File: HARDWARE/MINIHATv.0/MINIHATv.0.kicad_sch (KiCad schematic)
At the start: 9 parts, among them J1 USB_C_Receptacle_PowerOnly_6P, U1 MIC5504-3.3YM5

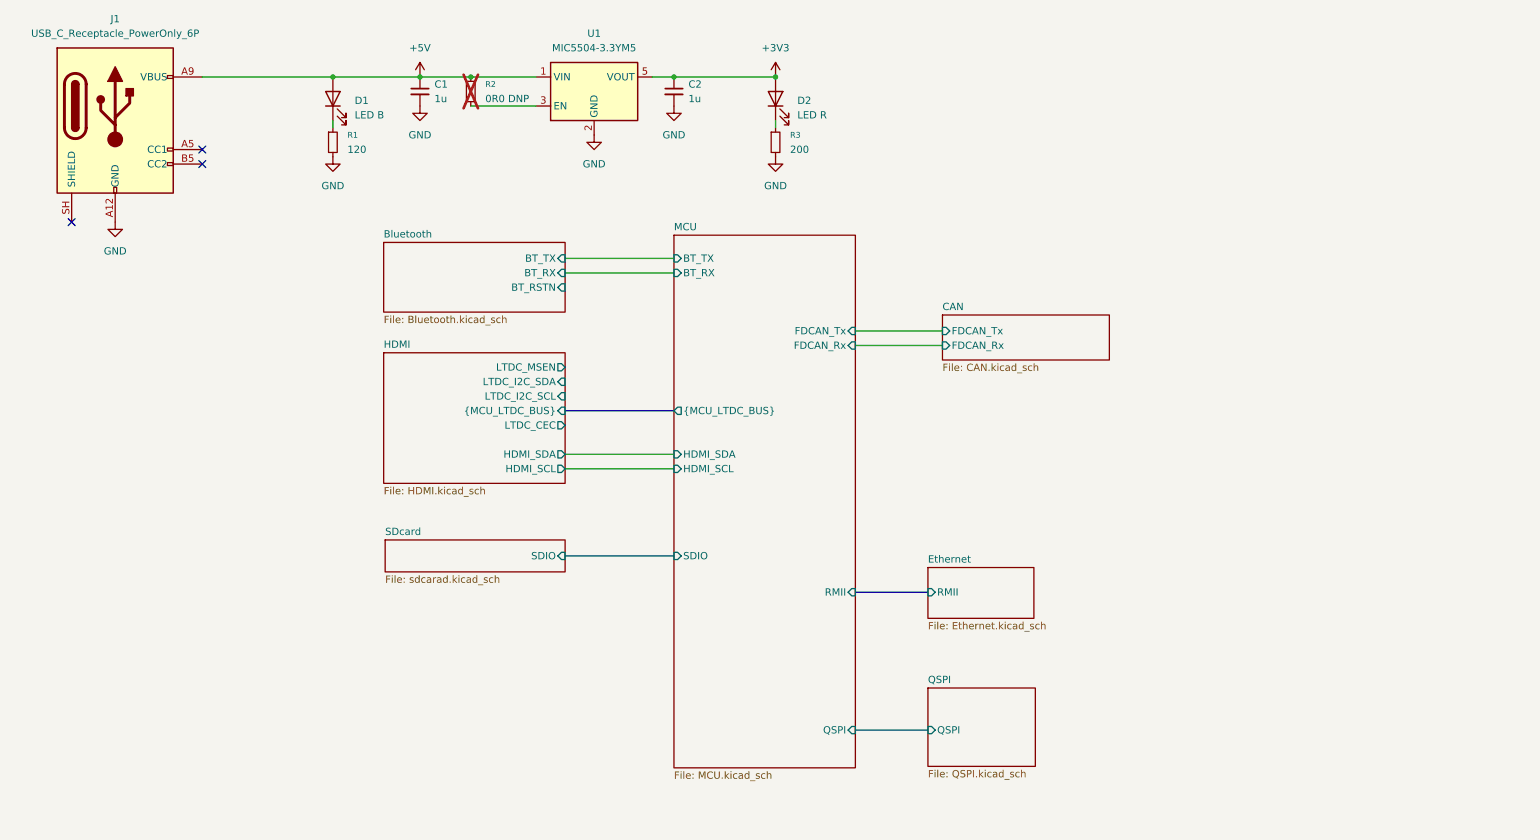
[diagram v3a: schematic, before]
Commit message: added sdram and usb pages to top page
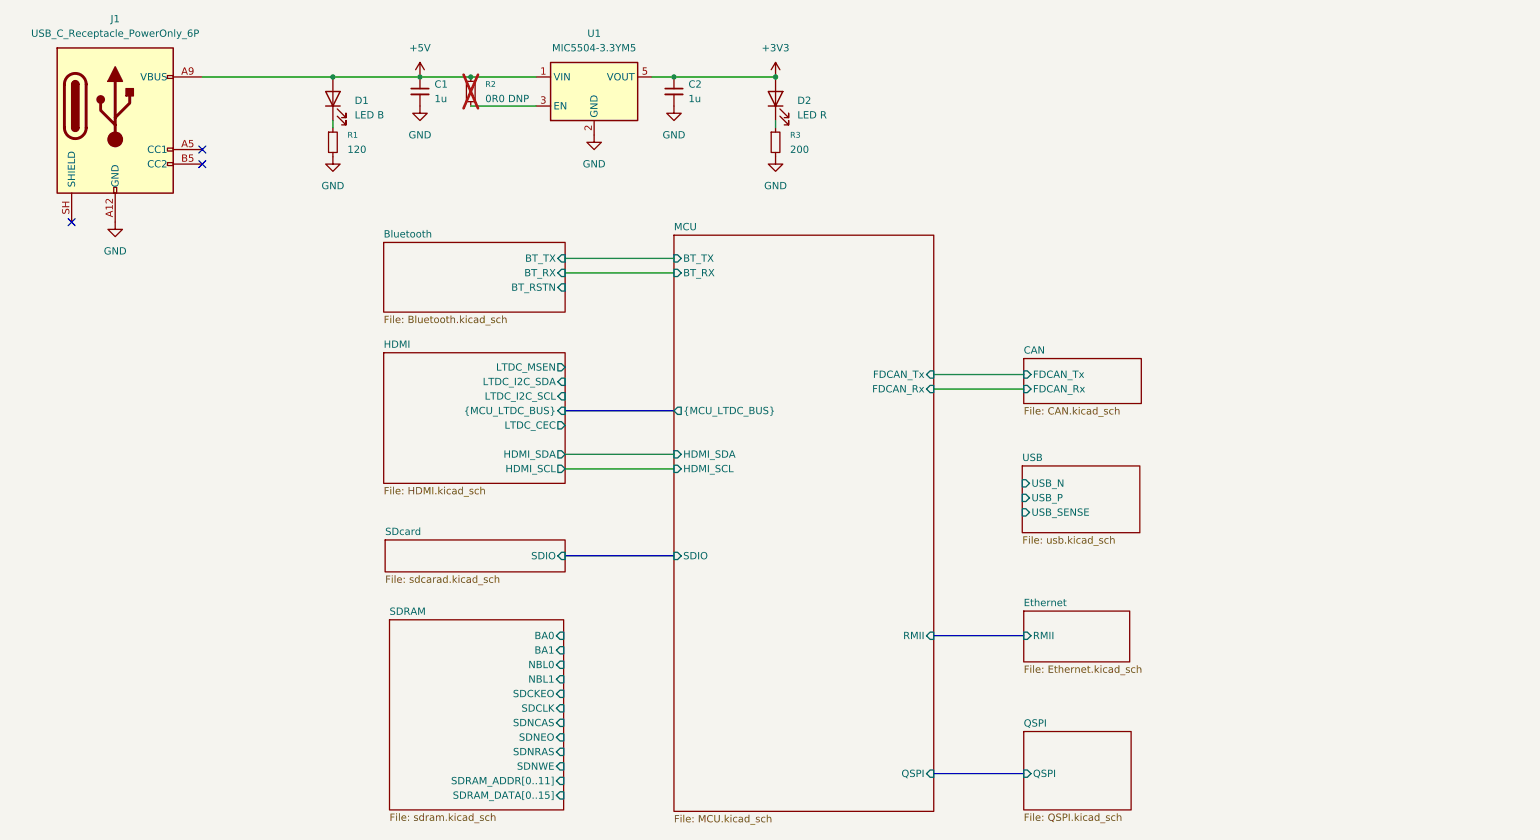
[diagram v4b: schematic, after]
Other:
- added sheet SDRAM (sdram.kicad_sch)
- added sheet USB (usb.kicad_sch)

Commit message: added ltdc bus to mcu page, editoral change to rmii bus
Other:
- sheet Ethernet ports: added ETH_RESET, {RMII}; removed RMII
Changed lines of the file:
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@@
 	(sheet
 		(at 189.484 117.602)
-		(size 18.542 8.89)
+		(size 18.542 10.922)
 		(exclude_from_sim no)
 		(in_bom yes)
@@
 		)
 		(property "Sheetfile" "Ethernet.kicad_sch"
-			(at 189.484 127.0766 0)
+			(at 189.484 129.1086 0)
 			(show_name no)
 			(do_not_autoplace no)
@@
 			)
 		)
-		(pin "RMII" input
+		(pin "ETH_RESET" input
+			(at 189.484 124.46 180)
+			(effects
+				(font
+					(size 1.27 1.27)
+				)
+				(justify left)
+			)
+		)
+		(pin "{RMII}" input
 			(at 189.484 121.92 180)
 			(effects

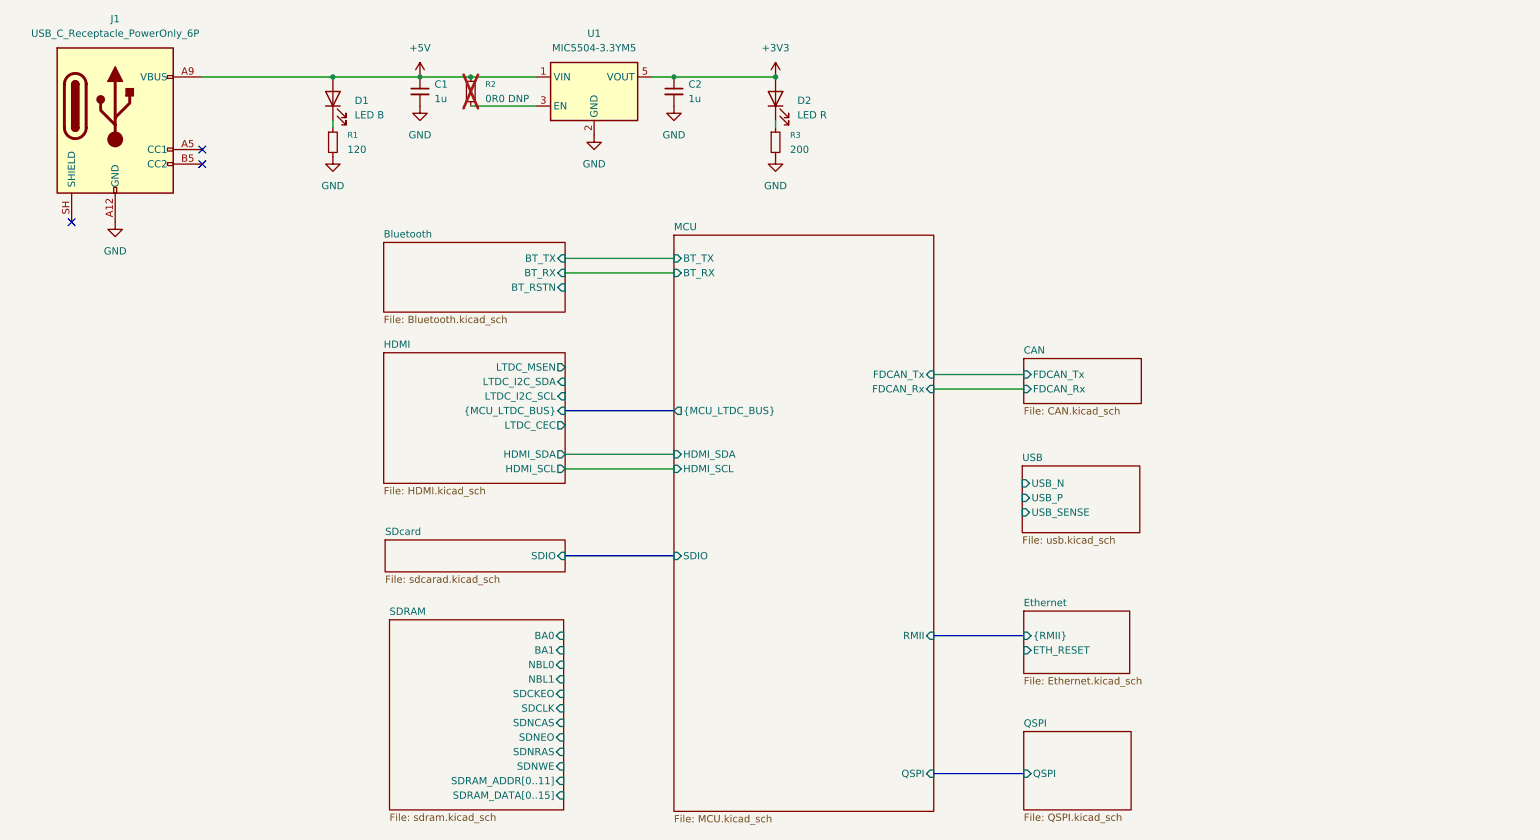
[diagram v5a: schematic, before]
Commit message: connecting i2c and uart bt/hdmi
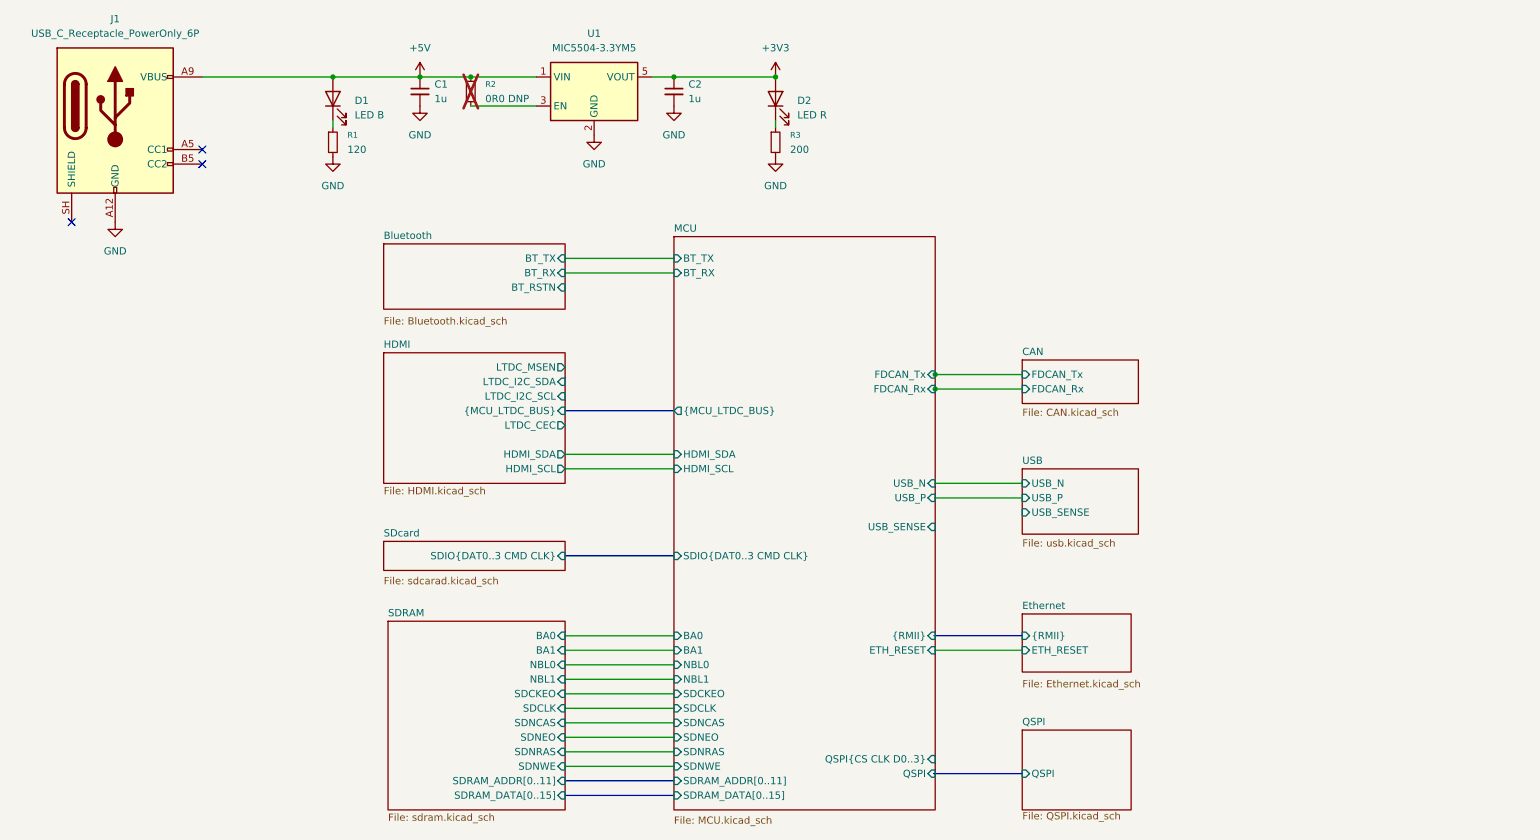
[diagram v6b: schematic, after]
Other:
- sheet MCU ports: added BA0, BA1, ETH_RESET, NBL0, NBL1, QSPI{CS CLK D0..3}, SDCKEO, SDCLK, SDIO{DAT0..3 CMD CLK}, SDNCAS, SDNEO, SDNRAS, SDNWE, SDRAM_ADDR[0..11], SDRAM_DATA[0..15], USB_N, USB_P, USB_SENSE, {RMII}; removed RMII, SDIO
- sheet SDcard ports: added SDIO{DAT0..3 CMD CLK}; removed SDIO

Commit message: mcu pwr/vcap ports, hdmi gpio, buses
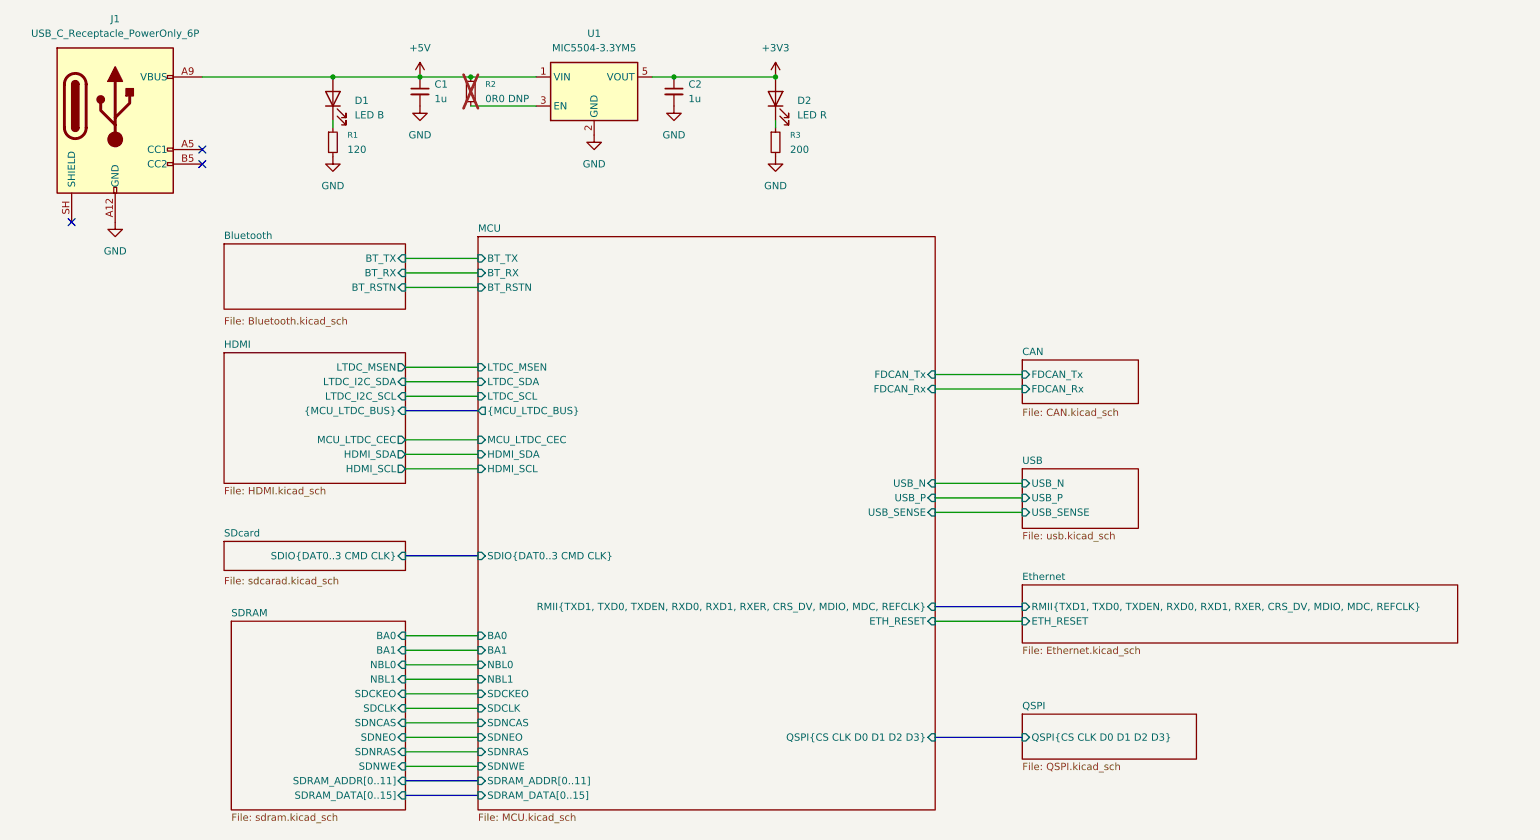
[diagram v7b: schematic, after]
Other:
- sheet Ethernet ports: added RMII{TXD1, TXD0, TXDEN, RXD0, RXD1, RXER, CRS_DV, MDIO, MDC, REFCLK}; removed {RMII}
- sheet HDMI ports: added MCU_LTDC_CEC; removed LTDC_CEC
- sheet MCU ports: added BT_RSTN, LTDC_MSEN, LTDC_SCL, LTDC_SDA, MCU_LTDC_CEC, QSPI{CS CLK D0 D1 D2 D3}, RMII{TXD1, TXD0, TXDEN, RXD0, RXD1, RXER, CRS_DV, MDIO, MDC, REFCLK}; removed QSPI, QSPI{CS CLK D0..3}, {RMII}
- sheet QSPI ports: added QSPI{CS CLK D0 D1 D2 D3}; removed QSPI

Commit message: audio page added to top
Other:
- added sheet Audio (audio.kicad_sch)
- sheet MCU ports: added I2S{CLK DIN DOUT WS}; removed none
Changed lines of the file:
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@@
+		)
+	)
+	(bus
+		(pts
+			(xy 173.99 59.69) (xy 187.96 59.69)
+		)
+		(stroke
+			(width 0)
+			(type default)
 		)
 	)
@@
 			)
 		)
+		(pin "I2S{CLK DIN DOUT WS}" input
+			(at 173.99 59.69 0)
+			(effects
+				(font
+					(size 1.27 1.27)
+				)
+				(justify right)
+			)
+		)
 		(instances
 			(project "MINIHATv.0"
@@
 				)
 			)
+		)
+	)
+	(sheet
+		(at 187.96 53.34)
+		(size 26.67 12.7)
+		(exclude_from_sim no)
+		(in_bom yes)
+		(on_board yes)
+		(dnp no)
+		(fields_autoplaced yes)
+		(stroke
+			(width 0.1524)
+			(type solid)
+		)
+		(fill
+			(color 0 0 0 0)
+		)
+		(property "Sheetname" "Audio"
+			(at 187.96 52.6284 0)
+			(show_name no)
+			(do_not_autoplace no)
+			(effects
+				(font
+					(size 1.27 1.27)
+				)
+				(justify left bottom)
+			)
+		)
+		(property "Sheetfile" "audio.kicad_sch"
+			(at 187.96 66.6246 0)
+			(show_name no)
+			(do_not_autoplace no)
+			(effects
+				(font
+					(size 1.27 1.27)
+				)
+				(justify left top)
+			)
+		)
+		(pin "I2S{CLK DIN DOUT WS}" input
+			(at 187.96 59.69 180)
+			(effects
+				(font
+					(size 1.27 1.27)
+				)
+				(justify left)
+			)
+		)
+		(instances
+			(project "MINIHATv.0"
+				(path "/19041ef4-1d16-4363-8780-721ad9f20b33"
+					(page "11")
+				)
+			)
